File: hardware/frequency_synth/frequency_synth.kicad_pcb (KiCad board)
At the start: 4 copper layers, 97.1 x 32.8 mm, 278 parts, among them P1001 CONN_01X02, Q1001 DMG2305UX, U1001 boosterpack_ti, U1002 CONN_SMA_2GND, U1003 ADM7150, U1004 picture, U201 CONN_SMA_2GND, U202 LMX2592, U203 CONN_SMA_2GND, U204 CONN_SMA_2GND, U205 CONN_SMA_2GND, U304 HMC321, U305 HMC321, U401 LTC1983, U402 HMC424, U403 74HC04_FULL, U601 PE42521, U901 LMK61E2

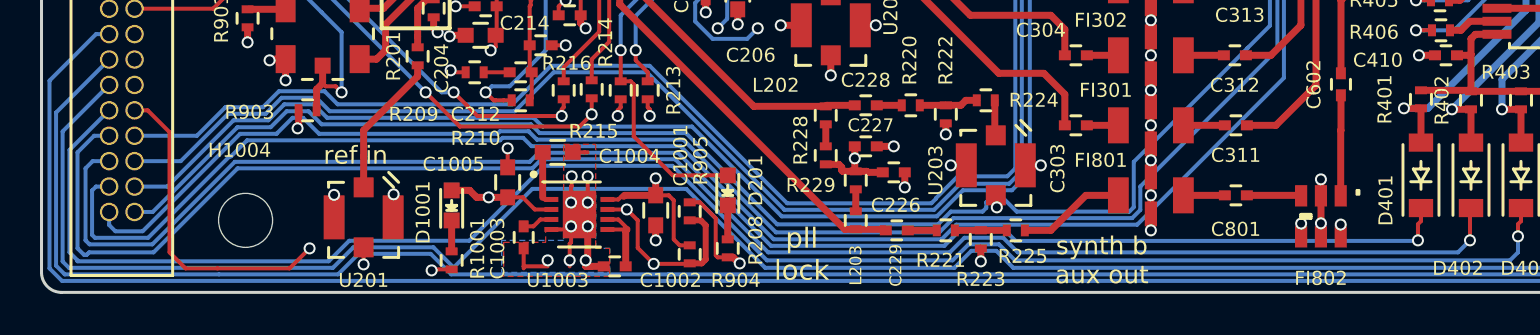
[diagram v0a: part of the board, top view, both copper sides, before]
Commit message: fixed footprints for filters on synth board
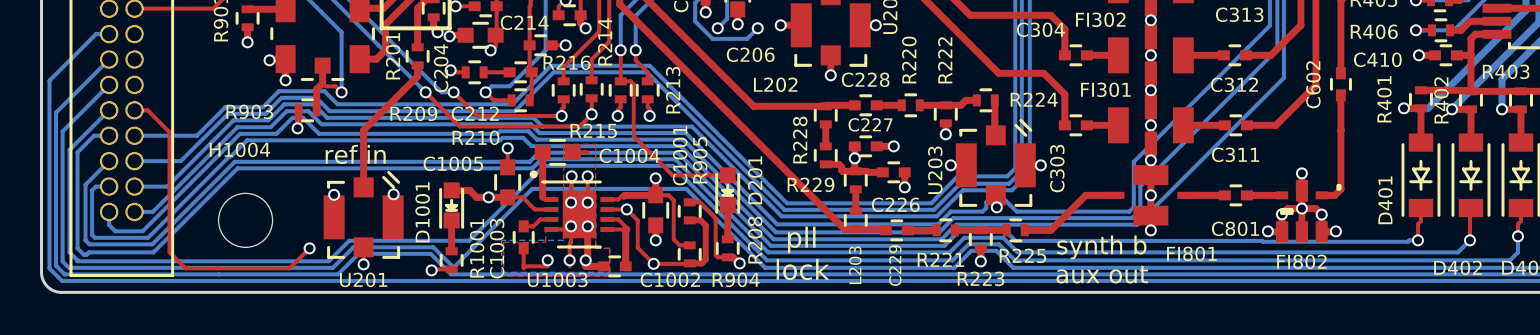
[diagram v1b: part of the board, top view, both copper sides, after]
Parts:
- D401, D402, D403, D404, D405, D406: value 3.3V -> 5.1V
- FI801: footprint vna_footprints:FV1206 -> vna_footprints:FV1206-4
- FI802: footprint vna_footprints:FV1206-1 -> vna_footprints:FV1206-1_p35mm_ustrip
- moved FI802 0.98 mm to (223.8, 112.5)
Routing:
- net GND: track 170.3 -> 174.5 mm, vias 130 -> 132
- net Net-(C801-Pad1): track 2.77 -> 1.81 mm
- net /switch/SW_RF1: track 5.03 -> 5.80 mm
